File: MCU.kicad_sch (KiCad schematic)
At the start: 22 parts, among them IC2 ESP32-C3FH4, Y1 40 Mhz Crystal

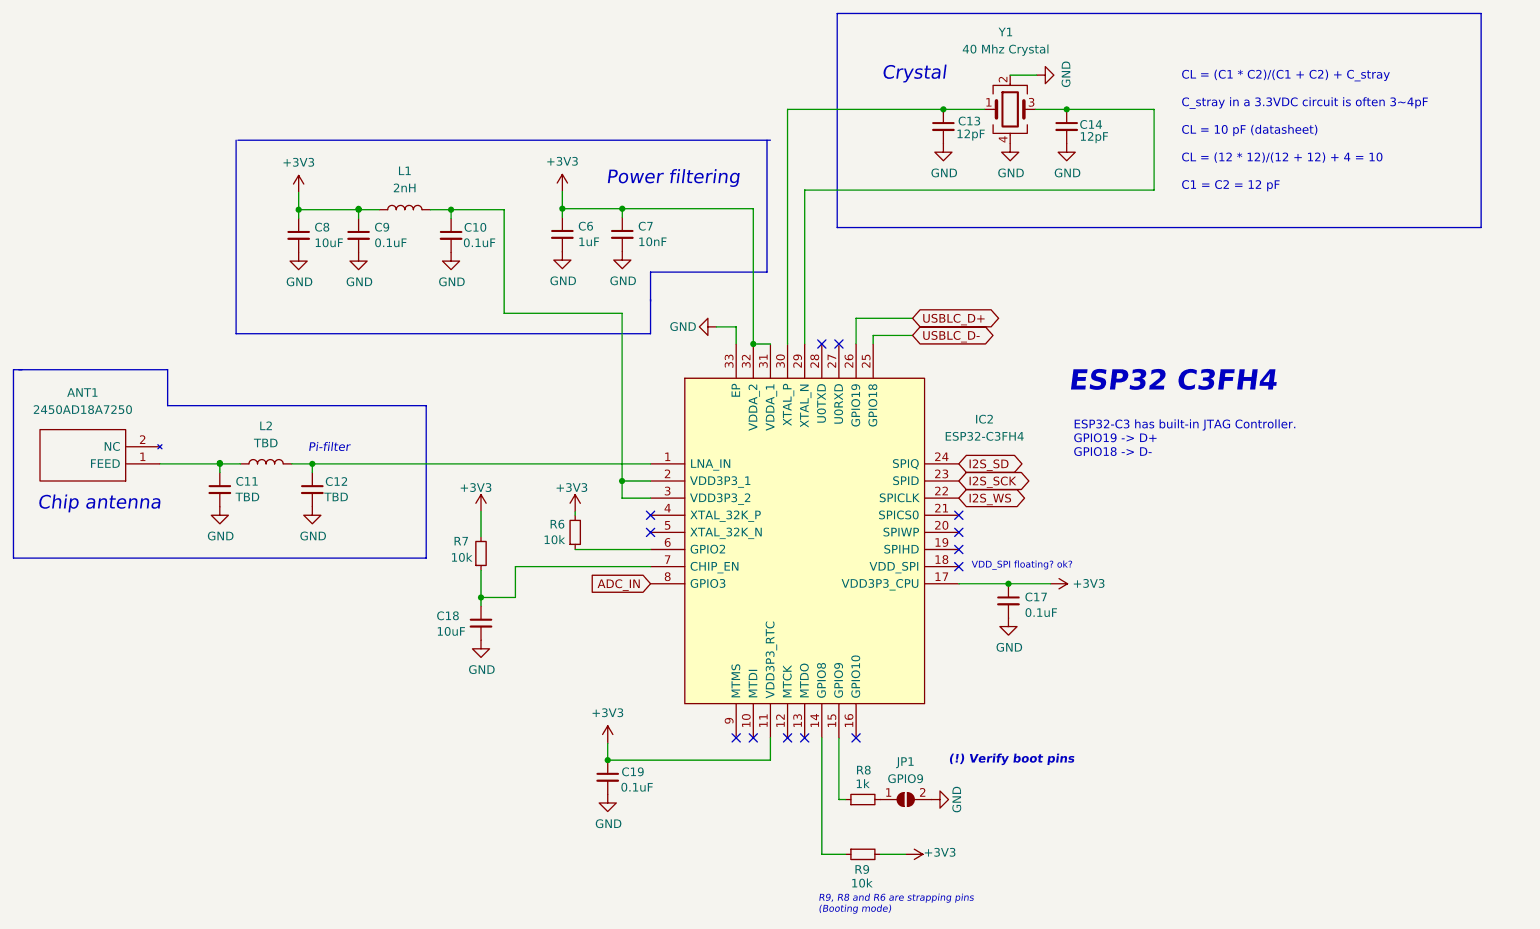
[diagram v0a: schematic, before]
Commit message: Added accelerometer
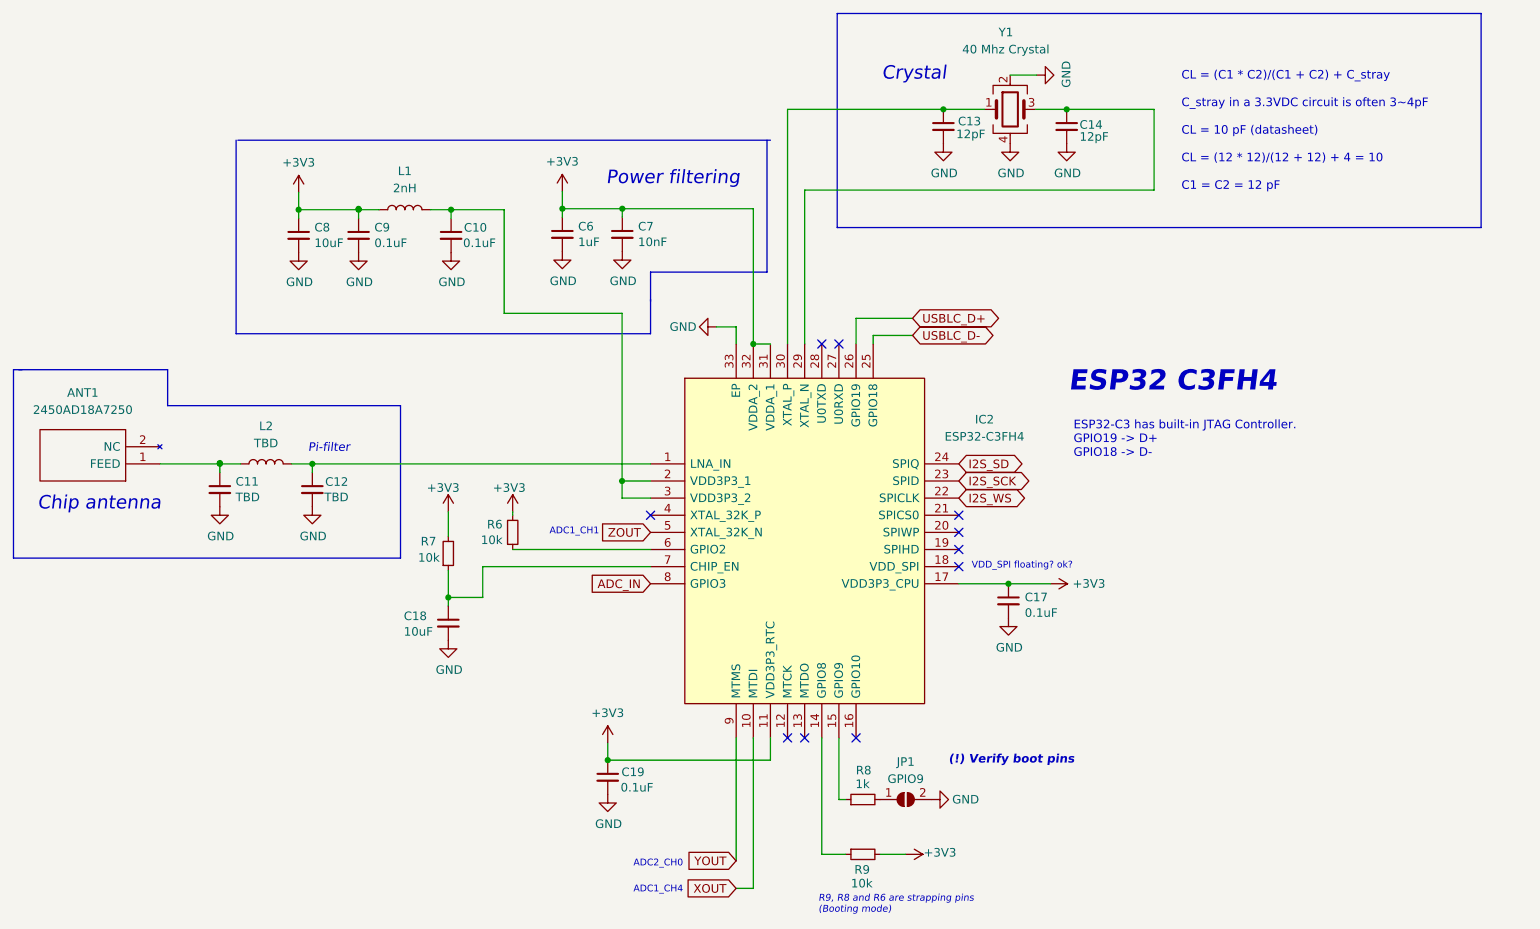
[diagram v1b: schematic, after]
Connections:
- net XOUT: now reaches IC2.10 (MTDI)
- net ZOUT: now reaches IC2.5 (XTAL_32K_N)
- net YOUT: now reaches IC2.9 (MTMS)
- no-connect marks 13 -> 10
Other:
- note added: "ADC1_CH1"
- note added: "ADC1_CH4"
- note added: "ADC2_CH0"
- moved on the sheet: C18, R6, R7

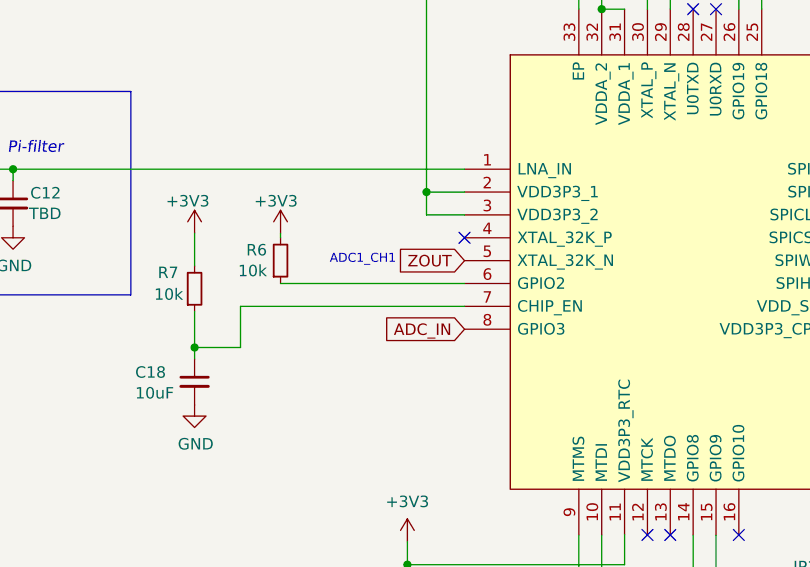
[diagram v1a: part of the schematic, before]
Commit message: Made new layout
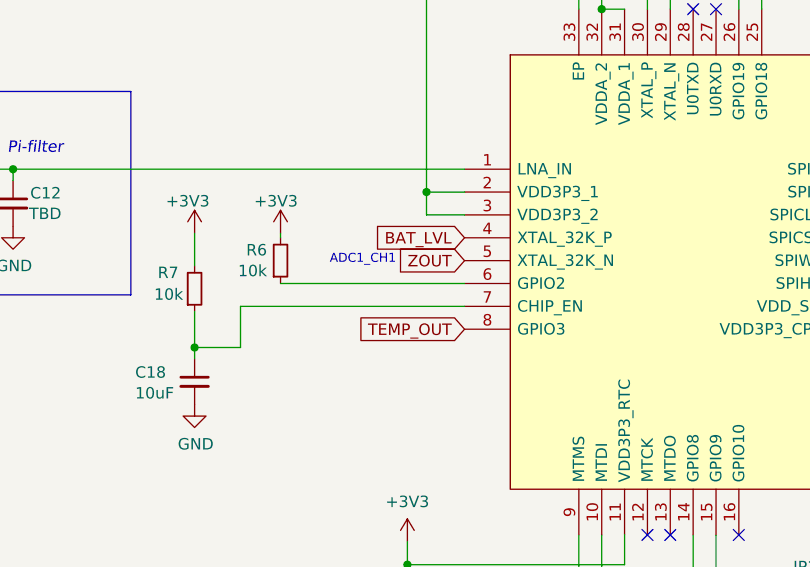
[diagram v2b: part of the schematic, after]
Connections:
- net BAT_LVL: now reaches IC2.4 (XTAL_32K_P)
- net ADC_IN renamed TEMP_OUT
- no-connect marks 10 -> 9
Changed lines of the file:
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@@
   (no_connect (at 147.828 78.232))
   (no_connect (at 145.288 136.652))
-  (no_connect (at 122.428 103.632))
   (no_connect (at 168.148 108.712))
   (no_connect (at 168.148 103.632))
@@
     )
   )
-  (global_label "ADC_IN" (shape input) (at 122.428 113.792 180) (fields_autoplaced)
-    (effects (font (size 1.27 1.27)) (justify right))
-    (property "Intersheet References" "${INTERSHEET_REFS}" (id 0) (at 113.5724 113.7126 0)
-      (effects (font (size 1.27 1.27)) (justify right) hide)
-    )
+  (global_label "TEMP_OUT" (shape input) (at 122.428 113.792 180) (fields_autoplaced)
+    (effects (font (size 1.27 1.27)) (justify right))
+    (property "Intersheet References" "${INTERSHEET_REFS}" (id 0) (at 110.6695 113.7126 0)
+      (effects (font (size 1.27 1.27)) (justify right) hide)
+    )
+  )
+  (global_label "BAT_LVL" (shape input) (at 122.428 103.632 180) (fields_autoplaced)
+    (effects (font (size 1.27 1.27)) (justify right))
+    (property "Intersheet References" "${INTERSHEET_REFS}" (id 0) (at 112.6652 103.5526 0)
+      (effects (font (size 1.27 1.27)) (justify right) hide)
+    )
